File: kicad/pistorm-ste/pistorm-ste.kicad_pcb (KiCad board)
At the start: 4 copper layers, 100 x 43.5 mm, 31 parts, among them J1 Raspberry_Pi_2_3, J2 PLCC68_plug, J3 Conn_01x02_Male, U1 SN54CBTD3384, U2 SN74LVC16373, U3 SN74LVC16373, U4 EPM240T100, U5 SN74LVC16373, U6 SN74LVC16373, U7 SN54CBTD3384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

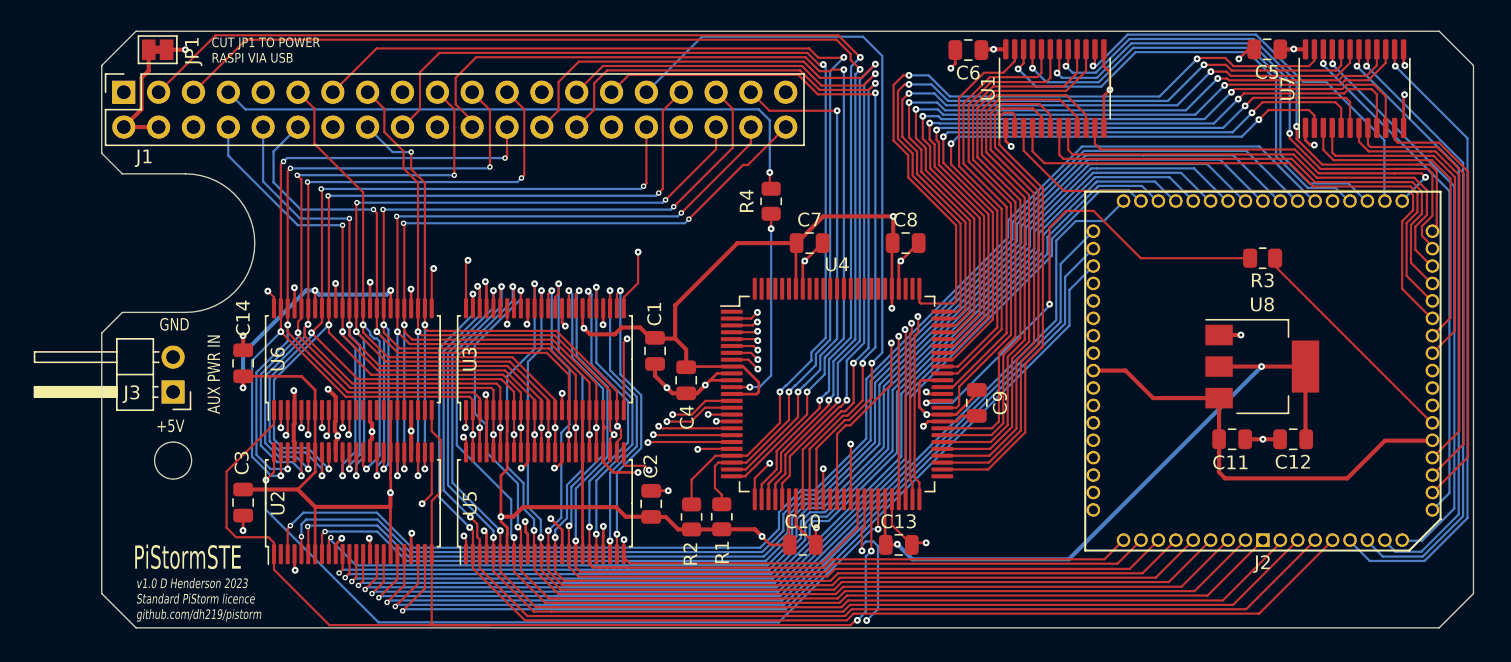
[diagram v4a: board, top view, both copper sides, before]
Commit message: Resized vias to hit another PCBWay price break
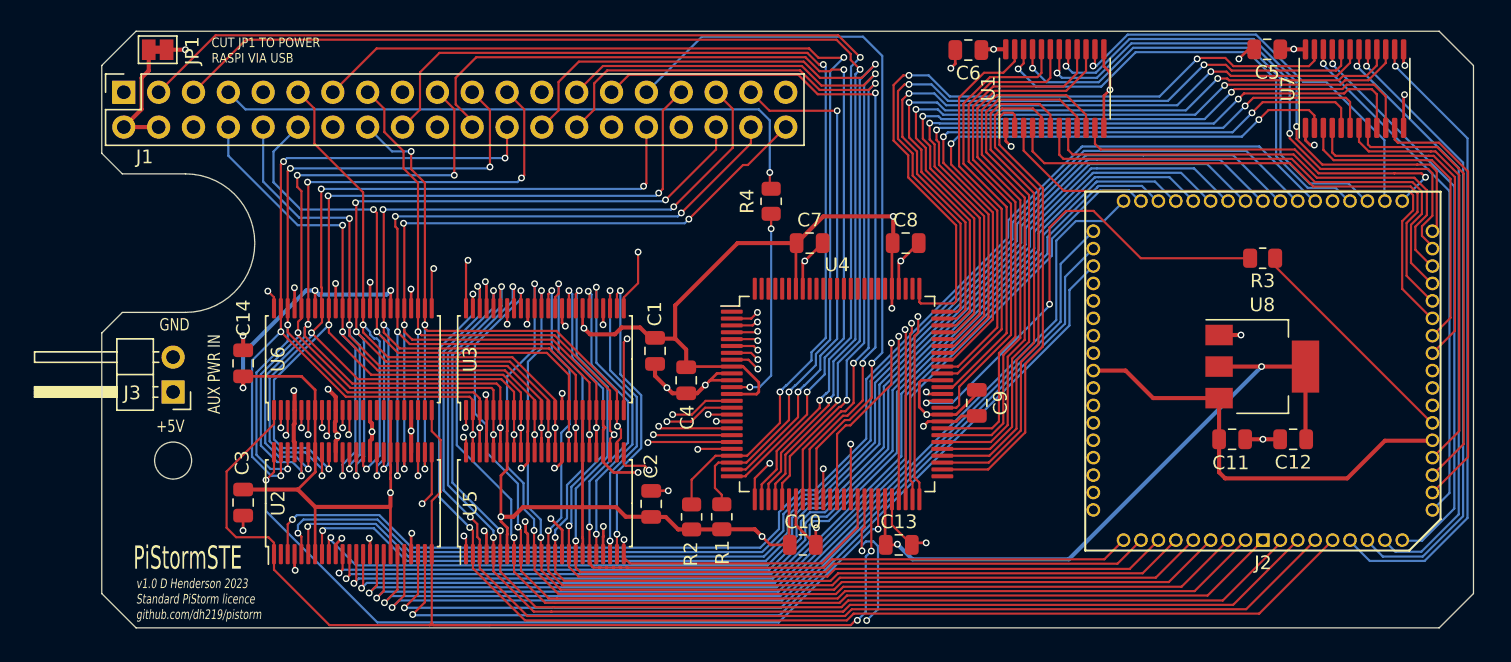
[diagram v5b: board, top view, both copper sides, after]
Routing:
- net /A14: track 68.2 -> 67.4 mm
- net /A15: track 67.1 -> 66.5 mm
